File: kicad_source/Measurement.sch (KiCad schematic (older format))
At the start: 25 parts, among them U6 OPA2374AIDCN, U7 OPA2374AIDCN, U8 ADS1015

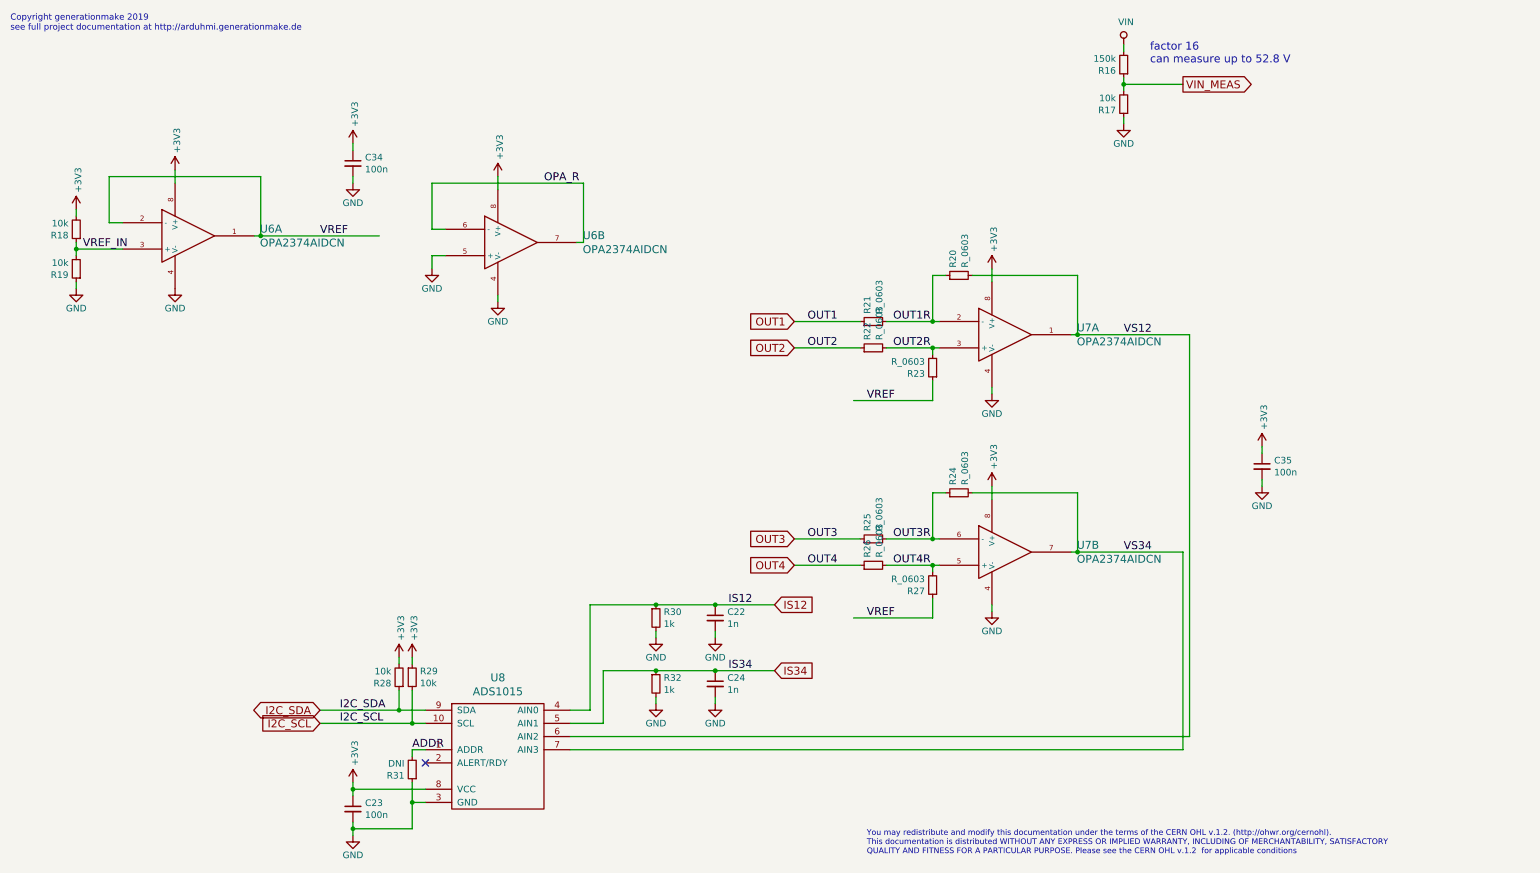
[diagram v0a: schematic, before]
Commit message: added values in schematic, generated pdf schematic
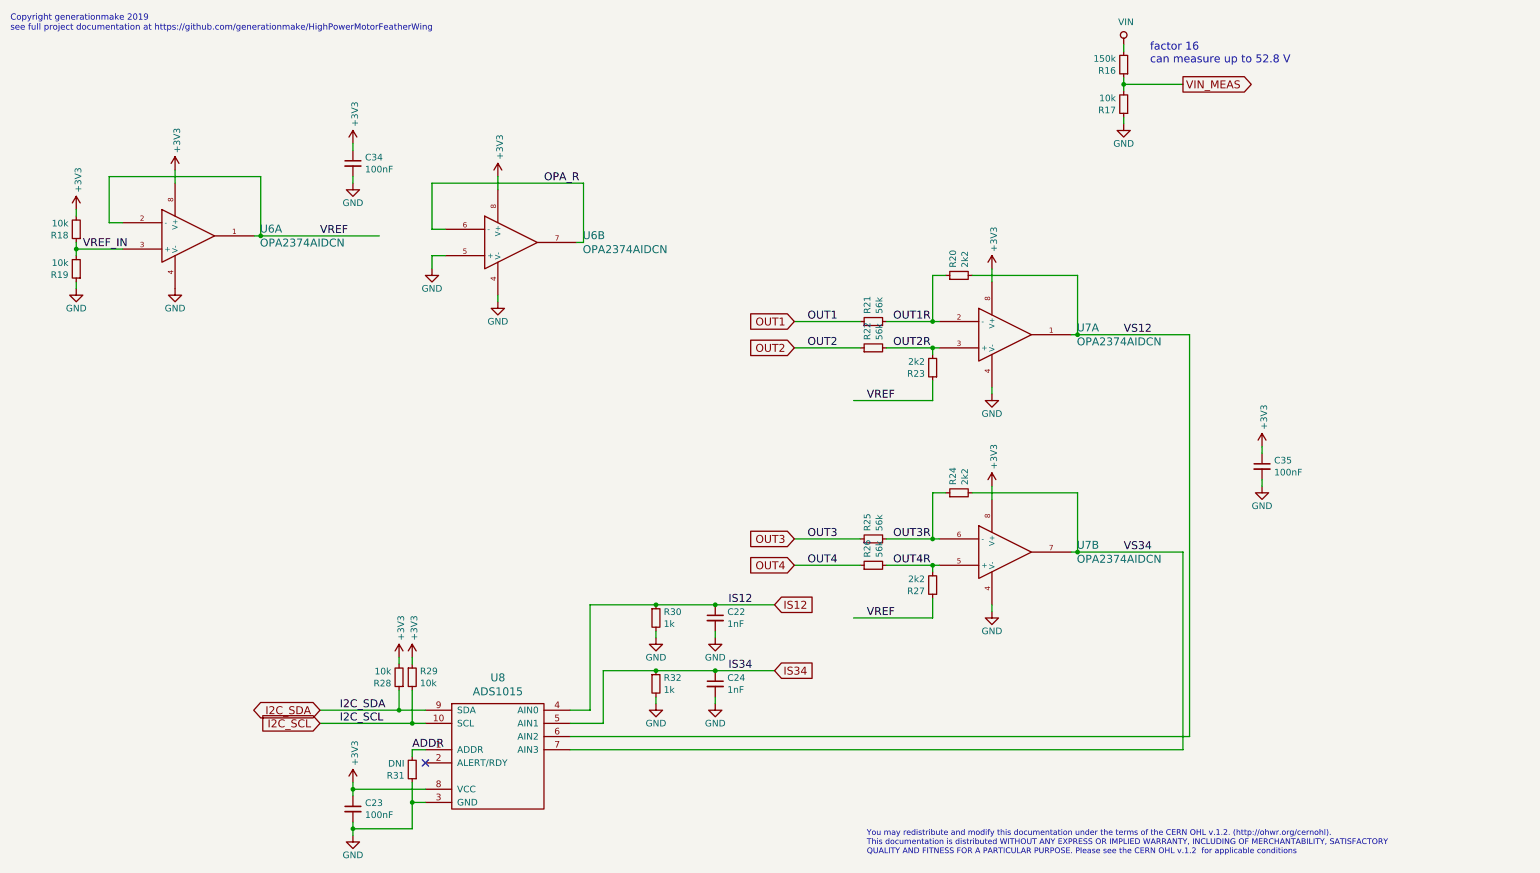
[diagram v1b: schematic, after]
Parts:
- C22, C24: value 1n -> 1nF
- C23, C34, C35: value 100n -> 100nF
- R20, R23, R24, R27: value R_0603 -> 2k2
- R21, R22, R25, R26: value R_0603 -> 56k
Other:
- note added: "Copyright generationmake 2019\nsee full project documentation at https://github.com/generationmake/HighPowerMotorFeatherWing"
- note removed: "Copyright generationmake 2019\nsee full project documentation at http://arduhmi.generationmake.de"
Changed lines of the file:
@@
 EESchema Schematic File Version 4
-LIBS:HighPowerMotorFeatherWing-cache
-EELAYER 26 0
+EELAYER 30 0
 EELAYER END
 $Descr A4 11693 8268
@@
 Sheet 3 5
 Title "HighPowerMotorFeatherWing"
-Date "2019-12-01"
+Date "2019-12-29"
 Rev "1.0"
 Comp "generationmake"
@@
 $EndDescr
 Text Notes 500  650  0    47   ~ 0
-Copyright generationmake 2019\nsee full project documentation at http://arduhmi.generationmake.de
+Copyright generationmake 2019\nsee full project documentation at https://github.com/generationmake/HighPowerMotorFeatherWing
 Text Notes 7000 6900 0    43   ~ 0
 You may redistribute and modify this documentation under the terms of the CERN OHL v.1.2. (http://ohwr.org/cernohl). \nThis documentation is distributed WITHOUT ANY EXPRESS OR IMPLIED WARRANTY, INCLUDING OF MERCHANTABILITY, SATISFACTORY \nQUALITY AND FITNESS FOR A PARTICULAR PURPOSE. Please see the CERN OHL v.1.2  for applicable conditions
@@
 P 3100 6550
 F 0 "C23" H 3192 6596 50  0000 L CNN
-F 1 "100n" H 3192 6505 50  0000 L CNN
+F 1 "100nF" H 3192 6505 50  0000 L CNN
 F 2 "capacitors:C_0603" H 3100 6400 50  0001 C CNN
 F 3 "" H 3100 6550 50  0000 C CNN
@@
 P 5850 5600
 F 0 "C24" H 5942 5646 50  0000 L CNN
-F 1 "1n" H 5942 5555 50  0000 L CNN
+F 1 "1nF" H 5942 5555 50  0000 L CNN
 F 2 "capacitors:C_0603" H 5850 5450 50  0001 C CNN
 F 3 "" H 5850 5600 50  0000 C CNN
@@
 P 5850 5100
 F 0 "C22" H 5942 5146 50  0000 L CNN
-F 1 "1n" H 5942 5055 50  0000 L CNN
+F 1 "1nF" H 5942 5055 50  0000 L CNN
 F 2 "capacitors:C_0603" H 5850 4950 50  0001 C CNN
 F 3 "" H 5850 5100 50  0000 C CNN
@@
 P 7500 3200
 F 0 "R23" H 7559 3246 50  0000 L CNN
-F 1 "R_0603" H 7559 3155 50  0000 L CNN
+F 1 "2k2" H 7559 3155 50  0000 L CNN
 F 2 "resistors:R_0603" H 7500 3050 50  0001 C CNN
 F 3 "" H 7500 3200 50  0000 C CNN
@@
 P 7050 3050
 F 0 "R22" H 7109 3096 50  0000 L CNN
-F 1 "R_0603" H 7109 3005 50  0000 L CNN
+F 1 "56k" H 7109 3005 50  0000 L CNN
 F 2 "resistors:R_0603" H 7050 2900 50  0001 C CNN
 F 3 "" H 7050 3050 50  0000 C CNN
@@
 P 7050 2850
 F 0 "R21" H 7109 2896 50  0000 L CNN
-F 1 "R_0603" H 7109 2805 50  0000 L CNN
+F 1 "56k" H 7109 2805 50  0000 L CNN
 F 2 "resistors:R_0603" H 7050 2700 50  0001 C CNN
 F 3 "" H 7050 2850 50  0000 C CNN
@@
 P 7700 2500
 F 0 "R20" H 7759 2546 50  0000 L CNN
-F 1 "R_0603" H 7759 2455 50  0000 L CNN
+F 1 "2k2" H 7759 2455 50  0000 L CNN
 F 2 "resistors:R_0603" H 7700 2350 50  0001 C CNN
 F 3 "" H 7700 2500 50  0000 C CNN
@@
 P 7500 4850
 F 0 "R27" H 7559 4896 50  0000 L CNN
-F 1 "R_0603" H 7559 4805 50  0000 L CNN
+F 1 "2k2" H 7559 4805 50  0000 L CNN
 F 2 "resistors:R_0603" H 7500 4700 50  0001 C CNN
 F 3 "" H 7500 4850 50  0000 C CNN
@@
 P 7050 4700
 F 0 "R26" H 7109 4746 50  0000 L CNN
-F 1 "R_0603" H 7109 4655 50  0000 L CNN
+F 1 "56k" H 7109 4655 50  0000 L CNN
 F 2 "resistors:R_0603" H 7050 4550 50  0001 C CNN
 F 3 "" H 7050 4700 50  0000 C CNN
@@
 P 7050 4500
 F 0 "R25" H 7109 4546 50  0000 L CNN
-F 1 "R_0603" H 7109 4455 50  0000 L CNN
+F 1 "56k" H 7109 4455 50  0000 L CNN
 F 2 "resistors:R_0603" H 7050 4350 50  0001 C CNN
 F 3 "" H 7050 4500 50  0000 C CNN
@@
 P 7700 4150
 F 0 "R24" H 7759 4196 50  0000 L CNN
-F 1 "R_0603" H 7759 4105 50  0000 L CNN
+F 1 "2k2" H 7759 4105 50  0000 L CNN
 F 2 "resistors:R_0603" H 7700 4000 50  0001 C CNN
 F 3 "" H 7700 4150 50  0000 C CNN
@@
 P 3100 1650
 F 0 "C34" H 3192 1696 50  0000 L CNN
-F 1 "100n" H 3192 1605 50  0000 L CNN
+F 1 "100nF" H 3192 1605 50  0000 L CNN
 F 2 "capacitors:C_0603" H 3100 1500 50  0001 C CNN
 F 3 "" H 3100 1650 50  0000 C CNN
@@
 P 10000 3950
 F 0 "C35" H 10092 3996 50  0000 L CNN
-F 1 "100n" H 10092 3905 50  0000 L CNN
+F 1 "100nF" H 10092 3905 50  0000 L CNN
 F 2 "capacitors:C_0603" H 10000 3800 50  0001 C CNN
 F 3 "" H 10000 3950 50  0000 C CNN
